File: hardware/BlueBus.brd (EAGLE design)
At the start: 90 x 55 mm, 73 parts

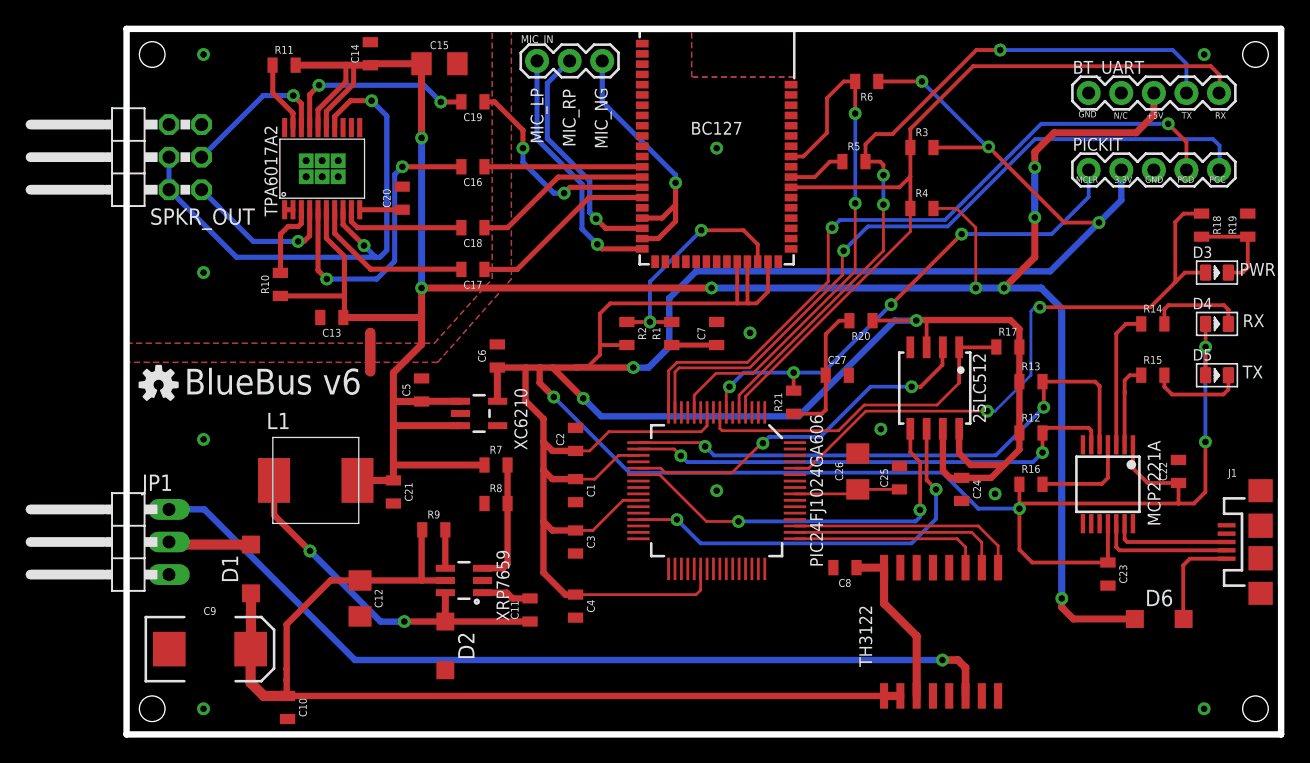
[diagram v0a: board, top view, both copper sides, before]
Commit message: [IMP] hardware: Silkscreen / Power rail update * Adjust silkscreen text for PICKIT to locate it below the pins, rather than under * Remove 45 degree angles from 3.3v rail to PIC24 * Remove skew from the VIN wiring near the 100uF cap
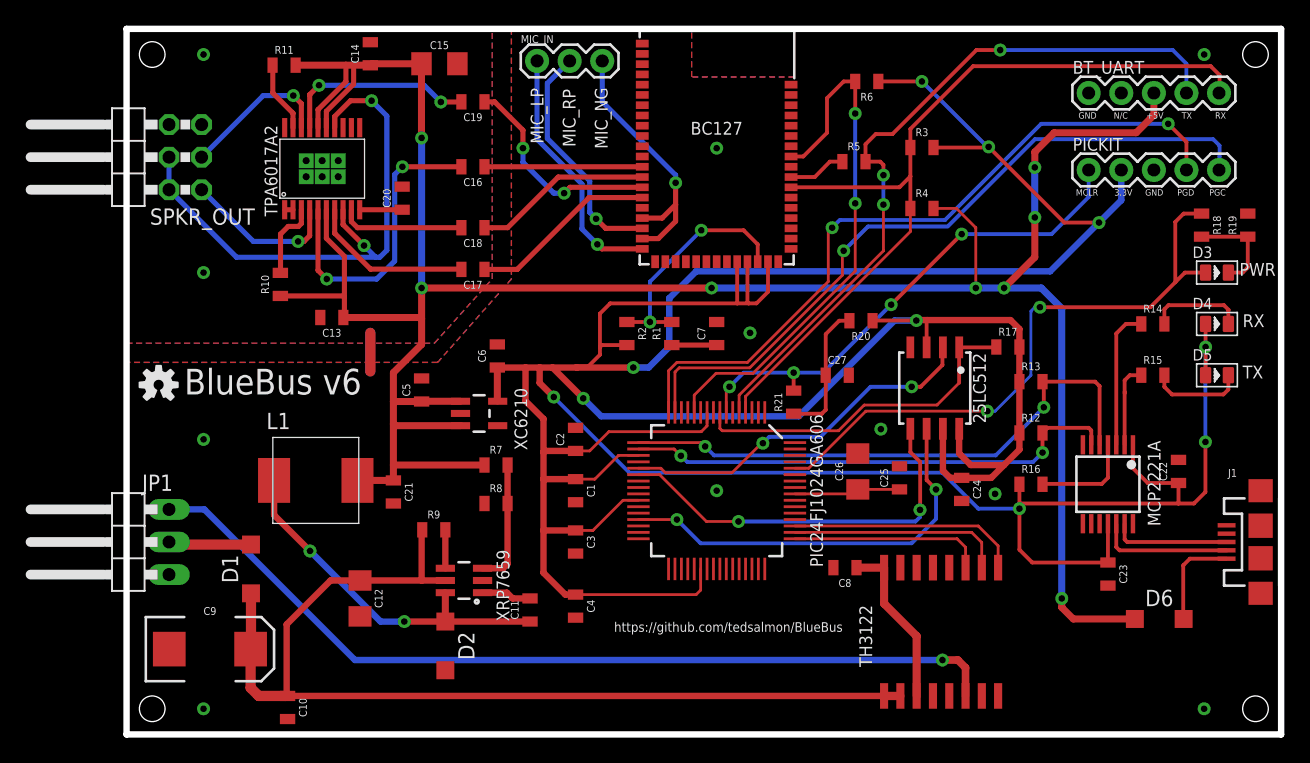
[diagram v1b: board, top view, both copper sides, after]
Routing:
- net 3.3V: track 349.4 -> 348.6 mm
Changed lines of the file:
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@@
 <text x="87" y="31.75" size="1" layer="25">RX</text>
 <text x="87" y="27.75" size="1" layer="25">TX</text>
-<text x="74.2" y="48.1" size="0.5" layer="25">GND</text>
+<text x="74.2" y="48" size="0.5" layer="25">GND</text>
 <text x="76.95" y="48" size="0.5" layer="25">N/C</text>
 <text x="79.5" y="48" size="0.5" layer="25">+5V</text>
 <text x="82.25" y="48" size="0.5" layer="25">TX</text>
 <text x="84.85" y="48" size="0.5" layer="25">RX</text>
-<text x="74" y="43" size="0.5" layer="25">MCLR</text>
-<text x="77" y="43" size="0.5" layer="25">3.3V</text>
-<text x="79.4" y="43" size="0.5" layer="25">GND</text>
-<text x="81.9" y="43" size="0.5" layer="25">PGD</text>
-<text x="84.4" y="43" size="0.5" layer="25">PGC</text>
+<text x="74" y="42" size="0.5" layer="25">MCLR</text>
+<text x="77" y="42" size="0.5" layer="25">3.3V</text>
+<text x="79.4" y="42" size="0.5" layer="25">GND</text>
+<text x="81.9" y="42" size="0.5" layer="25">PGD</text>
+<text x="84.4" y="42" size="0.5" layer="25">PGC</text>
 <text x="8.5" y="17.15" size="1" layer="26" rot="MR0">IBUS</text>
 <text x="8.5" y="14.65" size="1" layer="26" rot="MR0">VIN</text>
@@
 <hole x="88" y="53" drill="2"/>
 <hole x="2" y="2" drill="2"/>
-<text x="38" y="8" size="0.75" layer="51">https://github.com/tedsalmon/BlueBus</text>
+<text x="38" y="8" size="0.75" layer="25">https://github.com/tedsalmon/BlueBus</text>
 </plain>
 <attributes>
@@
 <wire x1="15.9" y1="12" x2="12.48" y2="8.58" width="0.5" layer="1"/>
 <wire x1="15.9" y1="12" x2="18.2" y2="12" width="0.5" layer="1"/>
+<wire x1="12.48" y1="8.58" x2="12.48" y2="3.07" width="0.5" layer="1"/>
+<wire x1="12.55" y1="3" x2="59.05" y2="3" width="0.5" layer="1"/>
+<wire x1="59.05" y1="3" x2="60.32" y2="3" width="0.65" layer="1"/>
+<wire x1="12.48" y1="3.07" x2="12.55" y2="3" width="0.5" layer="1"/>
+<wire x1="9.67" y1="6.65" x2="9.67" y2="3.63" width="0.8" layer="1"/>
+<wire x1="9.67" y1="3.63" x2="10.3" y2="3" width="0.8" layer="1"/>
+<wire x1="10.3" y1="3" x2="12.41" y2="3" width="0.8" layer="1"/>
+<wire x1="12.41" y1="3" x2="12.48" y2="3.07" width="0.8" layer="1"/>
 <wire x1="9.7" y1="11" x2="9.7" y2="6.68" width="0.8" layer="1"/>
 <wire x1="9.7" y1="6.68" x2="9.67" y2="6.65" width="0.8" layer="1"/>
-<wire x1="12.48" y1="8.58" x2="12.48" y2="5.1" width="0.5" layer="1"/>
-<wire x1="12.48" y1="5.1" x2="12.48" y2="4.23" width="0.5" layer="1"/>
-<wire x1="12.55" y1="3" x2="59.05" y2="3" width="0.5" layer="1"/>
-<wire x1="59.05" y1="3" x2="60.32" y2="3" width="0.65" layer="1"/>
-<wire x1="9.67" y1="6.65" x2="9.67" y2="4.03" width="0.8" layer="1"/>
-<wire x1="9.67" y1="4.03" x2="10.7" y2="3" width="0.8" layer="1"/>
-<wire x1="10.7" y1="3" x2="12.55" y2="3" width="0.8" layer="1"/>
-<wire x1="12.48" y1="4.23" x2="12.48" y2="3.07" width="0.5" layer="1"/>
-<wire x1="12.48" y1="3.07" x2="12.55" y2="3" width="0.5" layer="1"/>
 <wire x1="9.7" y1="11" x2="9.7" y2="14.8" width="0" layer="19" extent="1-1"/>
 </signal>
@@
 <wire x1="31.1" y1="28.6" x2="31.1" y2="26" width="0.5" layer="1"/>
 <wire x1="31.1" y1="26" x2="32.5" y2="24.6" width="0.5" layer="1"/>
-<wire x1="32.5" y1="24.6" x2="32.5" y2="22.8" width="0.5" layer="1"/>
-<wire x1="32.5" y1="22.8" x2="33.2" y2="22.1" width="0.5" layer="1"/>
-<wire x1="33.2" y1="22.1" x2="35" y2="22.1" width="0.5" layer="1"/>
-<wire x1="32.5" y1="22.8" x2="32.5" y2="20.6" width="0.5" layer="1"/>
-<wire x1="32.5" y1="20.6" x2="33.2" y2="19.9" width="0.5" layer="1"/>
-<wire x1="33.2" y1="19.9" x2="35" y2="19.9" width="0.5" layer="1"/>
-<wire x1="32.5" y1="16.6" x2="33.2" y2="15.9" width="0.5" layer="1"/>
-<wire x1="33.2" y1="15.9" x2="35" y2="15.9" width="0.5" layer="1"/>
 <wire x1="35" y1="22.1" x2="36.1" y2="22.1" width="0.22" layer="1"/>
 <wire x1="36.1" y1="22.1" x2="37.6" y2="23.6" width="0.22" layer="1"/>
@@
 <wire x1="61.565" y1="32.265" x2="58.165" y2="32.265" width="0.3" layer="1"/>
 <wire x1="58.165" y1="32.265" x2="58.15" y2="32.25" width="0.3" layer="1"/>
-<wire x1="32.5" y1="20.6" x2="32.5" y2="16.6" width="0.5" layer="1"/>
-<wire x1="32.5" y1="16.6" x2="32.5" y2="12.6" width="0.5" layer="1"/>
+<wire x1="32.5" y1="24.6" x2="32.5" y2="22" width="0.5" layer="1"/>
+<wire x1="32.5" y1="22" x2="32.5" y2="19.9" width="0.5" layer="1"/>
+<wire x1="32.5" y1="19.9" x2="32.5" y2="15.9" width="0.5" layer="1"/>
+<wire x1="32.5" y1="15.9" x2="32.5" y2="12.6" width="0.5" layer="1"/>
+<wire x1="35" y1="22.1" x2="32.6" y2="22.1" width="0.5" layer="1"/>
+<wire x1="32.6" y1="22.1" x2="32.5" y2="22" width="0.5" layer="1"/>
+<wire x1="35" y1="19.9" x2="32.5" y2="19.9" width="0.5" layer="1"/>
+<wire x1="35" y1="15.9" x2="32.5" y2="15.9" width="0.5" layer="1"/>
 </signal>
 <signal name="5V">

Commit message: [FIX] hardware: BlueBus v7 * Update Silkscreen for Speaker outputs * Rewire Speaker negative outputs to support single ended operation without overheating * Place 10uF cap for TPA6017A2 near input of 5v so all VDDs can benefit from it * Connect TPA6017A2 N/C pin to GND * Move TPA6017A2 gain resistor * Rewire transient filter for BC127 on the 3.3v rail per application note * Update placement of several passives for alignment * Update passive names to move from bottom right to left, to top right to left * Update Silkscreen with GitHub address
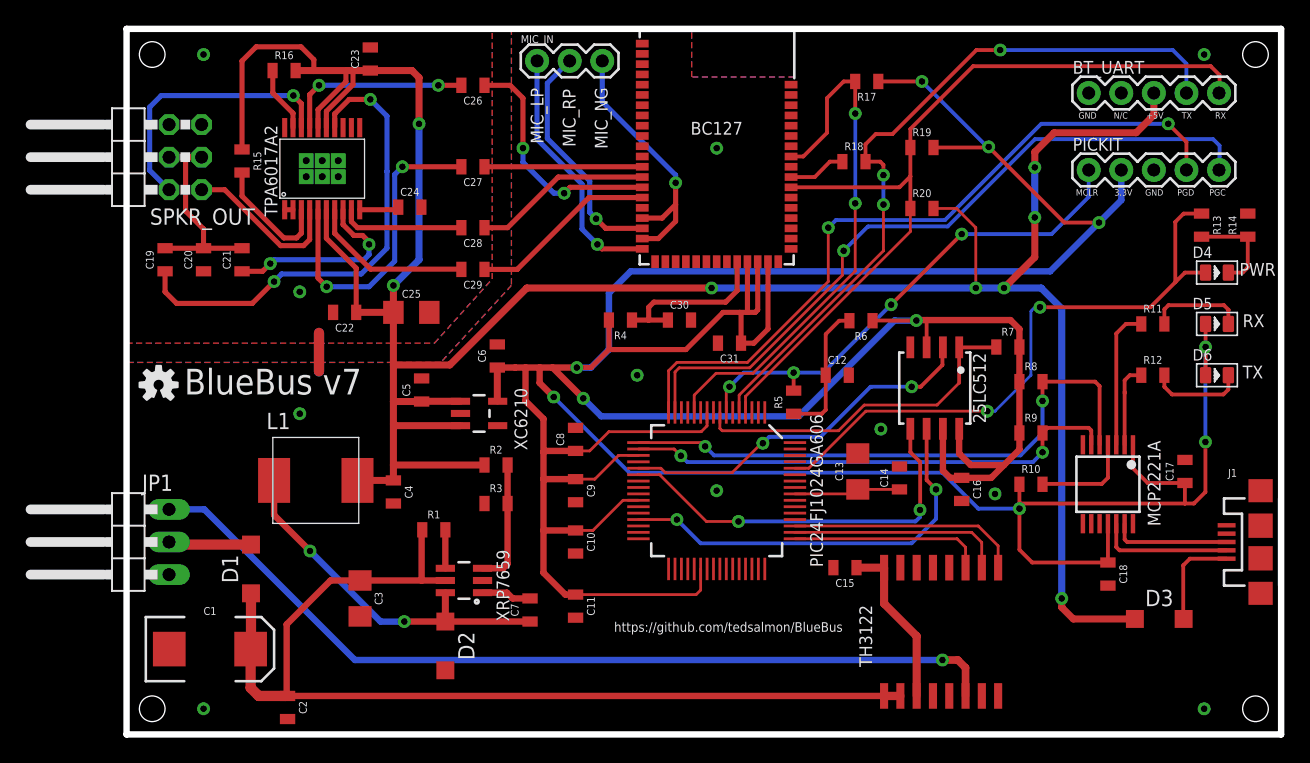
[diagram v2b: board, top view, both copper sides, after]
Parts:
- removed R21: 240, Passives:0805
- added C28, C29: 0.47uF, Passives:0805
- added C30: 4.7uF, Passives:0805
- added C31: 100nF, Passives:0805
- C1: value 0.1uF -> 100uF; device Passives:0805 -> Passives:EIA7343
- C10: value 47nF -> 0.1uF
- C11: value 0.01uF -> 0.1uF
- C12: value 10uF -> 0.1uF; device Passives:1206 -> Passives:0805
- C13: value 0.47uF -> 10uF; device Passives:0805 -> Passives:1206
- C14, C16, C17, C18: value 0.47uF -> 0.1uF
- C15: value 10uF -> 2.2uF; device Passives:1206 -> Passives:0805
- C19, C20: value 0.47uF -> (none)
- C2: value 0.1uF -> 47nF
- C21: value 22uF -> (none)
- C22, C23, C24, C27: value 0.1uF -> 0.47uF
- C25, C3: value 0.1uF -> 10uF; device Passives:0805 -> Passives:1206
- C26: value 10uF -> 0.47uF; device Passives:1206 -> Passives:0805
- C4: value 0.1uF -> 22uF
- C7: value 4.7uF -> 0.01uF
- C8: value 2.2uF -> 0.1uF
- C9: value 100uF -> 0.1uF; device Passives:EIA7343 -> Passives:0805
- D3: value GREEN-0805 -> 2A/100V; device Seeed-LED:LED-0805 -> Passives:SOD123
- D5: value RED-0805 -> GREEN-0805
- D6: value 2A/100V -> RED-0805; device Passives:SOD123 -> Seeed-LED:LED-0805
- R1: value 0.22 -> 100k
- R10: value 100k -> 10k
- R11, R12: value 100k -> 1k
- R13: value 100k -> 36k
- R14: value 1k -> 2k
- R15: value 1k -> 100k
- R16: value 10k -> 100k
- R17: value 5.1k -> 10k
- R18: value 36k -> 10k
- R19: value 2k -> 10k
- R2: value 0.75 -> 47k
- R3: value 10k -> 9.09k
- R4: value 10k -> 2k
- R5: value 10k -> 240
- R7: value 47k -> 5.1k
- R8: value 9.09k -> 100k
- moved R15 72.9 mm to (9.00, 44.7), turned to 270 degrees
- moved R11 70.7 mm to (80.0, 32.0)
- moved C23 70.1 mm to (19.0, 52.6), turned to 90 degrees
- moved R16 66.6 mm to (12.3, 51.8)
- moved C22 66.2 mm to (17.0, 32.9), turned to 180 degrees
- moved R10 60.5 mm to (70.5, 19.5), turned to 0 degrees
- moved C17 57.7 mm to (82.5, 20.5), turned to 90 degrees
- moved C18 56.4 mm to (76.5, 12.5), turned to 270 degrees
- moved C14 52.9 mm to (60.2, 20.0)
- moved C15 50.4 mm to (56.0, 13.0), turned to 180 degrees
- moved C24 48.3 mm to (22.1, 41.1), turned to 0 degrees
- moved R9 47.2 mm to (70.5, 23.5)
- moved C16 45.7 mm to (65.1, 19.1), turned to 270 degrees
- moved R3 43.3 mm to (28.8, 18.0)
- moved R8 42.8 mm to (70.5, 27.5)
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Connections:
- removed net BT_VBAT: BC127.32, R1.2, R2.1
- removed net SPKR_OUT_NEG: SPKR_OUT.2, SPKR_OUT.4, TPA6017A2.14, TPA6017A2.8
- removed net VBAT_CAP: C7.1, R1.1
- new net BT_VCHG: BC127.30, C30.1, R4.1
- new net SPKR_OUT_GND: C19.2, C20.2, C21.2, SPKR_OUT.3, SPKR_OUT.4
- new net SPKR_OUT_LN: C21.1, TPA6017A2.8
- new net SPKR_OUT_RN: C19.1, TPA6017A2.14
- net 3.3V: now also BC127.32, C10.1, C11.1, C16.1, C17.1, C18.1, C31.1, C8.1, C9.1, D6.+, R10.1, R17.1, R19.2, R4.2, R7.2, R8.1, R9.1; no longer BC127.30, C1.1, C2.1, C22.1, C23.1, C24.1, C3.1, C4.1, D4.+, R12.1, R13.1, R16.1, R17.2, R2.2, R20.1, R3.2
- net 5V: now also C22.1, C23.1, C25.1, C4.1, D3.C, R15.1, R16.2, R2.1, R20.2; no longer C13.1, C14.1, C15.1, C21.1, D6.C, R10.1, R11.2, R4.2, R7.1
- net BS: now also C7.2; no longer C11.2
- net BT_RESET: now also R17.2; no longer R6.2
- net BT_URX: now also R18.1, R18.2; no longer R5.1, R5.2
- net BT_UTX: now also R19.1, R20.1; no longer R3.1, R4.1
- net BYP: now also C24.1; no longer C20.1
- net EE_CS: now also R7.1; no longer R17.1
- net EN: now also R1.2; no longer R9.2
- net FB: now also R2.2, R3.2; no longer R7.2, R8.2
- net GAIN1: now also R15.2; no longer R10.2
- net GND: now also C1.C, C11.2, C16.2, C17.2, C18.2, C20.1, C30.2, C31.2, C9.2, R14.2, R3.1, TPA6017A2.12; no longer C1.2, C20.2, C21.2, C26.2, C27.2, C7.2, C9.C, R19.2, R8.1
- net MCP_5V: now also D3.A; no longer D6.A
- net MCP_LED0: now also R12.1; no longer R15.1
- net MCP_LED0_RES: now also D6.-, R12.2; no longer D5.-, R15.2
- net MCP_LED1: now also R11.1; no longer R14.1
- net MCP_LED1_RES: now also D5.-, R11.2; no longer D4.-, R14.2
- net MCP_RESET: now also R10.2; no longer R16.2
- net MCU_MCLR: now also R5.2; no longer R21.2
- net MCU_MCLR_PULL_UP: now also C12.1, R5.1, R6.2; no longer C27.1, R20.2, R21.1
- net ON_LED: now also D4.+, R13.1; no longer D3.+, R18.1
- net ON_LED_RES: now also D4.-, R13.2, R14.1; no longer D3.-, R18.2, R19.1
- net SHDN: now also R16.1; no longer R11.1
- net SPKR_IN_LN: now also C27.1, C27.2; no longer C16.1, C16.2
- net SPKR_IN_LP: now also C28.1, C28.2; no longer C18.1, C18.2
- net SPKR_IN_RN: now also C26.1, C26.2; no longer C19.1, C19.2
- net SPKR_IN_RP: now also C29.1, C29.2; no longer C17.1, C17.2
- net SPKR_OUT_RP: now also SPKR_OUT.2; no longer SPKR_OUT.3
- net SW: now also C7.1; no longer C11.1
- net SYS_URX: now also R8.2; no longer R13.2
- net SYS_UTX: now also R9.2; no longer R12.2
- net VCAP: now also C13.1, C14.1; no longer C25.1, C26.1
- net VIN: now also C1.A, C2.1, C3.1, R1.1; no longer C10.1, C12.1, C9.A, R9.1
- net VTR: now also C15.1; no longer C8.1
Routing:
- net SPKR_OUT_NEG: track 43.1 -> 0.00 mm, vias 2 -> 0
- net SPKR_OUT_RN: track 0.00 -> 37.5 mm, vias 0 -> 2
- net BT_VBAT: track 18.5 -> 0.00 mm, vias 2 -> 0
- net SPKR_OUT_GND: track 0.00 -> 16.2 mm
- net SPKR_OUT_LN: track 0.00 -> 15.2 mm, vias 0 -> 2
- net BT_VCHG: track 0.00 -> 13.5 mm
- net SPKR_OUT_RP: track 11.9 -> 21.4 mm
- net 5V: track 207.7 -> 216.4 mm
- net 3.3V: track 348.6 -> 355.2 mm
- net GAIN1: track 6.07 -> 9.79 mm
- net VBAT_CAP: track 3.50 -> 0.00 mm
- net SPKR_IN_RN: track 32.1 -> 33.6 mm
- net SYS_URX: track 44.8 -> 45.8 mm
- net SPKR_IN_LN: track 36.1 -> 36.9 mm
- net SPKR_OUT_LP: track 12.3 -> 12.8 mm, vias 1 -> 0
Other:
- board text added: "BlueBus v7"
- board text added: "NEG"
- board text removed: "BlueBus v6"
- board text removed: "L-"
- board text removed: "R-"
